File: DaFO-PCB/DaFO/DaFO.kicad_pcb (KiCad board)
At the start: 4 copper layers, 36 x 52 mm, 33 parts, among them J1 HTSW-104-X-X-S, J2 CES-104-X-X-S, J3 1862042

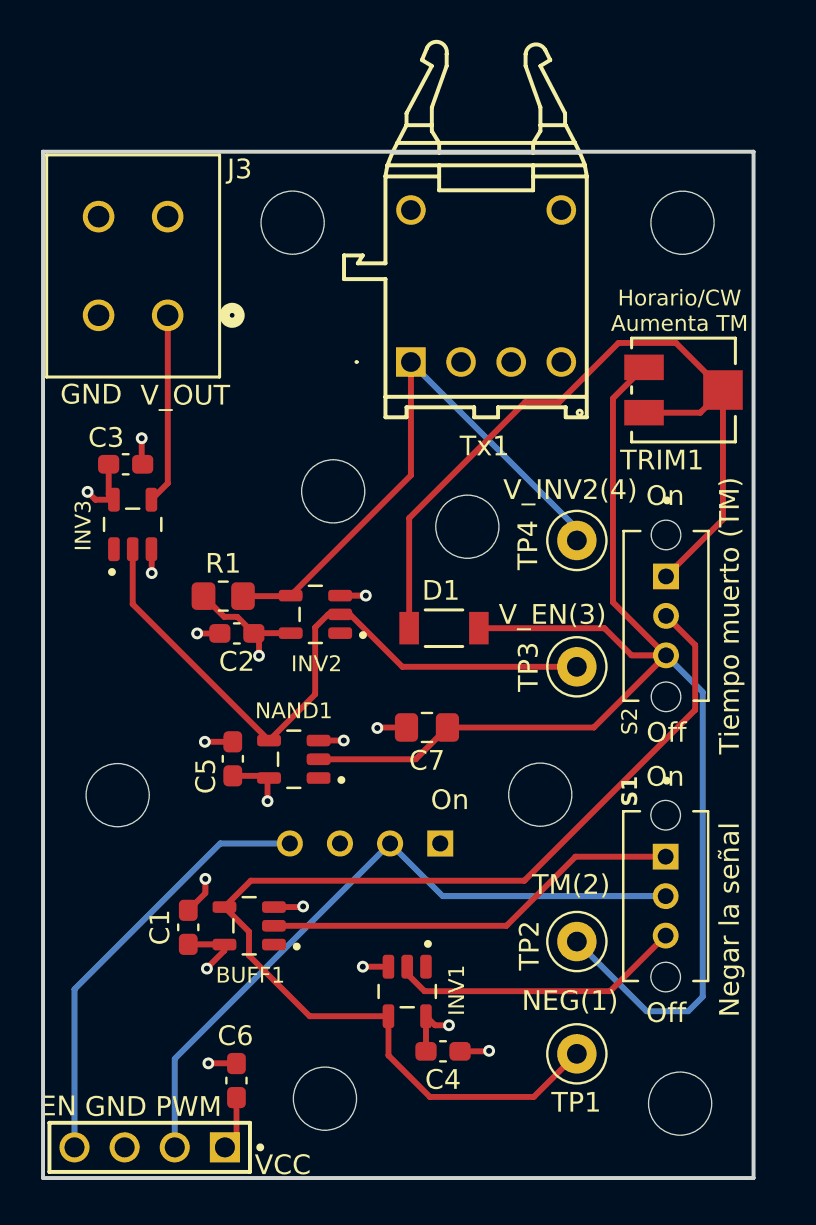
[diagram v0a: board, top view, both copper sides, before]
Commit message: Cambios para reducir tamaño y a componentes laterales. Creación de archivos de fabricación.
Se realizaron cambios a la PCB para reducir su tamaño, se cambiaron ciertos componentes y se tienen los archivos de fabricación de la placa.
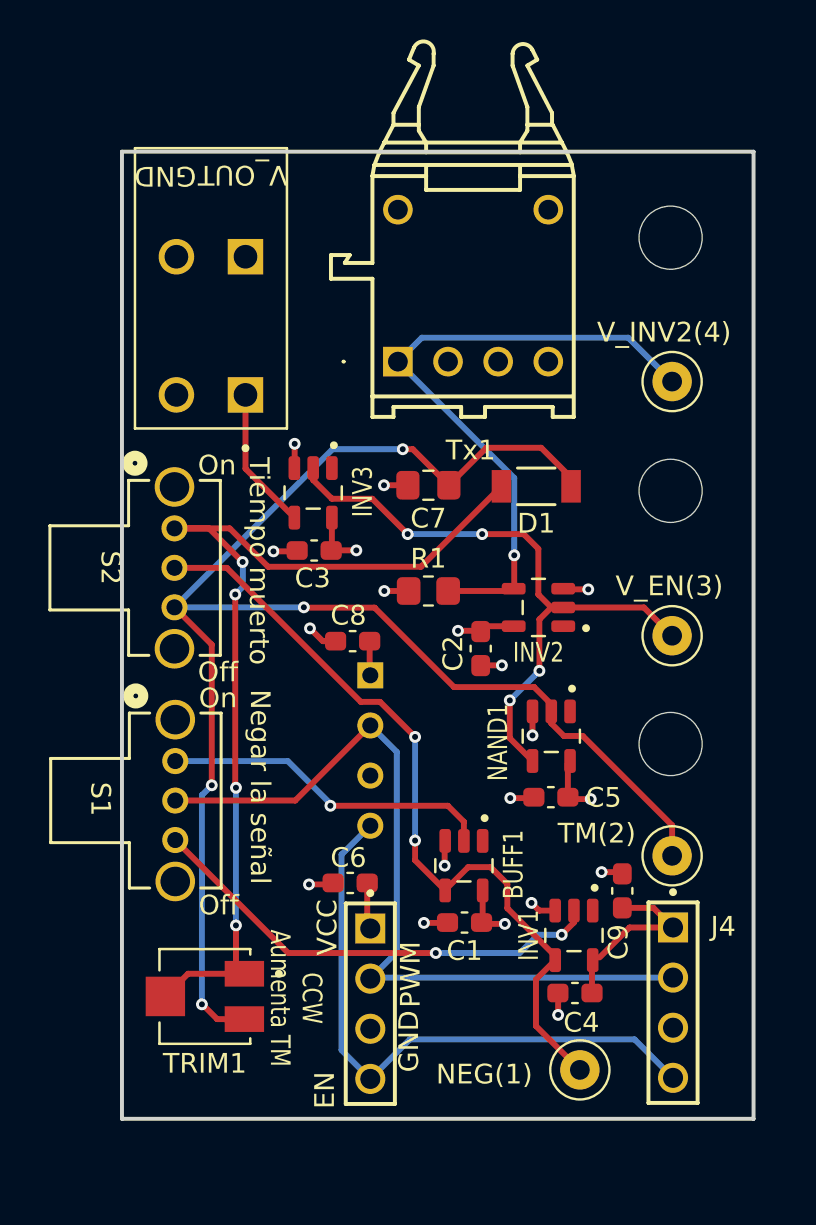
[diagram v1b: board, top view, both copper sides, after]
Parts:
- removed H4, H5, H6, H7, H8: MountingHole, MountingHole:MountingHole_3.2mm_M3
- removed J3: 1862042, CON_1862042:CONN_1862042
- added C8: 0.1u, Capacitor_SMD:C_0603_1608Metric_Pad1.08x0.95mm_HandSolder, F.Cu at (191.7, 70.1)
- added C9: 0.1u, Capacitor_SMD:C_0603_1608Metric_Pad1.08x0.95mm_HandSolder, F.Cu at (205.3, 82.7)
- added G***: LOGO, logo_gato:logo_gato, B.Cu at (185.6, 88.7)
- added J4: HTSW-104-X-X-S, SAMTEC_HTSW-104-X-X-S:SAMTEC_HTSW-104-X-X-S, F.Cu at (207.9, 88.4)
- added J5: TBLH10-350-02BK, CON_TBLH10_350_02BK:CUI_TBLH10-350-02BK, F.Cu at (186.3, 57.6)
- S1, S2: footprint SW_OS102011MS2QN1:SW_OS102011MS2QN1 -> SWITCH_OS102011MA1QN1:OS102011MA1QN1_CNK
- TRIM1: footprint TS53YJ_VIS:TS53YJ_VIS -> TRIM_3214J:TRIM_3214J-1-203E
- moved TRIM1 39.1 mm to (184.2, 88.1), turned to 180 degrees
- moved S1 25.8 mm to (182.7, 76.2)
- moved S2 25.3 mm to (182.7, 64.4)
- moved H1 21.4 mm to (207.8, 75.3)
- moved H2 16.7 mm to (207.8, 62.5)
- moved C5 16.2 mm to (201.7, 78.0), turned to 180 degrees
- moved C1 14.0 mm to (197.4, 84.3), turned to 180 degrees
- moved J1 13.3 mm to (192.6, 88.4), turned to 90 degrees
- moved NAND1 13.1 mm to (201.8, 74.9), turned to -90 degrees
- moved C2 12.4 mm to (198.2, 70.5), turned to -90 degrees
- moved C7 12.3 mm to (195.5, 62.2)
- moved C6 11.6 mm to (191.6, 82.3), turned to 180 degrees
- moved INV2 11.3 mm to (201.1, 68.4)
- moved BUFF1 11.3 mm to (197.3, 81.5), turned to -90 degrees
- moved C3 10.5 mm to (189.7, 65.5), turned to 180 degrees
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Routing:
- net /NEG: track 58.0 -> 39.9 mm, vias 0 -> 2
- net Net-(INV1-Pad2): track 15.0 -> 24.2 mm, vias 0 -> 2
- net /TM: track 72.4 -> 81.5 mm, vias 0 -> 4
- net /EN: track 22.0 -> 31.0 mm
- net Net-(D1-Pad1): track 41.7 -> 49.1 mm, vias 0 -> 4
- net /PWM: track 35.0 -> 40.8 mm
- net Net-(BUFF1-A): track 21.3 -> 16.9 mm, vias 0 -> 1
- net VCC: track 22.3 -> 26.2 mm
- net /V_INV2: track 29.5 -> 32.6 mm, vias 0 -> 1
- net Net-(J5-1): track 9.69 -> 7.25 mm
- net /V_EN: track 33.9 -> 32.5 mm, vias 0 -> 4
- net GND: track 16.8 -> 17.5 mm, vias 12 -> 14
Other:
- board size 36 x 52 mm -> 32 x 49 mm
- board text added: "CCW Aumenta TM"
- board text added: "Tiempo muerto"
- board text removed: "Horario/CW Aumenta TM"
